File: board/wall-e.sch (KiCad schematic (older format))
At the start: 61 parts, among them J1 Raspberry_Pi_2_3, J10 PCA9685, J11 VL53L0X, J12 VL53L0X, J13 VL53L0X, J14 MotorDrv2, J15 Motor2, J16 IMU, J17 INA219, J18 INA219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

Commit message: Move power monitors onto logic power.
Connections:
- net +5V: now also J17.1 (Pin_1), J18.1 (Pin_1)
- net +5VP: no longer J17.1 (Pin_1), J18.1 (Pin_1)
- net GND: now also J17.2 (Pin_2), J18.2 (Pin_2)
- net GNDA: no longer J17.2 (Pin_2), J18.2 (Pin_2)
- net I2C_ISO_SCL: no longer J17.3 (Pin_3), J18.3 (Pin_3)
- net I2C_ISO_SDA: no longer J17.4 (Pin_4), J18.4 (Pin_4)
- net I2C_M6_SCLK: now also J17.3 (Pin_3), J18.3 (Pin_3)
- net I2C_M6_SDA: now also J17.4 (Pin_4), J18.4 (Pin_4)
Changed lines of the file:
@@
 $EndComp
-$Comp
-L +5VP #PWR045
-U 1 1 5B72CC48
-P 7600 5850
-F 0 "#PWR045" H 7600 5700 50  0001 C CNN
-F 1 "+5VP" H 7600 5990 50  0000 C CNN
-F 2 "" H 7600 5850 50  0001 C CNN
-F 3 "" H 7600 5850 50  0001 C CNN
-	1    7600 5850
-	1    0    0    -1
-$EndComp
-$Comp
-L GNDA #PWR046
-U 1 1 5B72CCD2
-P 7550 6000
-F 0 "#PWR046" H 7550 5750 50  0001 C CNN
-F 1 "GNDA" H 7550 5850 50  0000 C CNN
-F 2 "" H 7550 6000 50  0001 C CNN
-F 3 "" H 7550 6000 50  0001 C CNN
-	1    7550 6000
-	0    1    1    0
-$EndComp
-Text GLabel 7650 6250 0    60   BiDi ~ 0
-I2C_ISO_SDA
-Text GLabel 7650 6150 0    60   Input ~ 0
-I2C_ISO_SCL
 $Comp
 L Conn_01x04 J18
@@
 Text Notes 9300 6300 0    60   ~ 0
 Vcc\nGND\nSCL\nSDA
-$Comp
-L +5VP #PWR047
-U 1 1 5B72DD15
-P 8900 5850
-F 0 "#PWR047" H 8900 5700 50  0001 C CNN
-F 1 "+5VP" H 8900 5990 50  0000 C CNN
-F 2 "" H 8900 5850 50  0001 C CNN
-F 3 "" H 8900 5850 50  0001 C CNN
-	1    8900 5850
-	1    0    0    -1
-$EndComp
-$Comp
-L GNDA #PWR048
-U 1 1 5B72DD1B
-P 8850 6000
-F 0 "#PWR048" H 8850 5750 50  0001 C CNN
-F 1 "GNDA" H 8850 5850 50  0000 C CNN
-F 2 "" H 8850 6000 50  0001 C CNN
-F 3 "" H 8850 6000 50  0001 C CNN
-	1    8850 6000
-	0    1    1    0
-$EndComp
-Text GLabel 8950 6250 0    60   BiDi ~ 0
-I2C_ISO_SDA
-Text GLabel 8950 6150 0    60   Input ~ 0
-I2C_ISO_SCL
 Text Notes 7750 5750 0    60   ~ 0
 Battery sensors\nDifferent addresses!
@@
 Wire Wire Line
 	2700 4500 2700 4600
+Text GLabel 7650 6150 0    60   Input ~ 0
+I2C_M6_SCLK
+Text GLabel 7650 6250 0    60   BiDi ~ 0
+I2C_M6_SDA
+Text GLabel 8950 6250 0    60   BiDi ~ 0
+I2C_M6_SDA
+Text GLabel 8950 6150 0    60   Input ~ 0
+I2C_M6_SCLK
+$Comp
+L +5V #PWR?
+U 1 1 5C045AF6
+P 7600 5850
+F 0 "#PWR?" H 7600 5700 50  0001 C CNN
+F 1 "+5V" H 7600 5990 50  0000 C CNN
+F 2 "" H 7600 5850 50  0001 C CNN
+F 3 "" H 7600 5850 50  0001 C CNN
+	1    7600 5850
+	1    0    0    -1
+$EndComp
+$Comp
+L +5V #PWR?
+U 1 1 5C045B84
+P 8900 5850
+F 0 "#PWR?" H 8900 5700 50  0001 C CNN
+F 1 "+5V" H 8900 5990 50  0000 C CNN
+F 2 "" H 8900 5850 50  0001 C CNN
+F 3 "" H 8900 5850 50  0001 C CNN
+	1    8900 5850
+	1    0    0    -1
+$EndComp
+$Comp
+L GND #PWR?
+U 1 1 5C045C8E
+P 7550 6000
+F 0 "#PWR?" H 7550 5750 50  0001 C CNN
+F 1 "GND" H 7550 5850 50  0000 C CNN
+F 2 "" H 7550 6000 50  0001 C CNN
+F 3 "" H 7550 6000 50  0001 C CNN
+	1    7550 6000
+	0    1    1    0
+$EndComp
+$Comp
+L GND #PWR?
+U 1 1 5C045D94
+P 8850 6000
+F 0 "#PWR?" H 8850 5750 50  0001 C CNN
+F 1 "GND" H 8850 5850 50  0000 C CNN
+F 2 "" H 8850 6000 50  0001 C CNN
+F 3 "" H 8850 6000 50  0001 C CNN
+	1    8850 6000
+	0    1    1    0
+$EndComp
 $EndSCHEMATC

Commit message: Tweaks.
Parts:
- added C15: 470u, Capacitors_THT:CP_Radial_D8.0mm_P3.50mm, symbol CP
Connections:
- net +5V: now also C15.1
- net GND: now also C15.2
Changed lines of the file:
@@
 Connection ~ 9850 2950
 $Comp
-L GND #PWR049
+L GND #PWR045
 U 1 1 5BF31737
 P 6050 7500
-F 0 "#PWR049" H 6050 7250 50  0001 C CNN
+F 0 "#PWR045" H 6050 7250 50  0001 C CNN
 F 1 "GND" H 6050 7350 50  0000 C CNN
 F 2 "" H 6050 7500 50  0001 C CNN
@@
 $EndComp
 $Comp
-L GNDA #PWR050
+L GNDA #PWR046
 U 1 1 5BF317C1
 P 6450 7500
-F 0 "#PWR050" H 6450 7250 50  0001 C CNN
+F 0 "#PWR046" H 6450 7250 50  0001 C CNN
 F 1 "GNDA" H 6450 7350 50  0000 C CNN
 F 2 "" H 6450 7500 50  0001 C CNN
@@
 	9750 2850 9800 2850
 $Comp
-L PWR_FLAG #FLG051
+L PWR_FLAG #FLG047
 U 1 1 5C026CFB
 P 7750 3450
-F 0 "#FLG051" H 7750 3525 50  0001 C CNN
+F 0 "#FLG047" H 7750 3525 50  0001 C CNN
 F 1 "PWR_FLAG" H 7750 3600 50  0000 C CNN
 F 2 "" H 7750 3450 50  0001 C CNN
@@
 Connection ~ 7650 3700
 $Comp
-L PWR_FLAG #FLG052
+L PWR_FLAG #FLG048
 U 1 1 5C027A7F
 P 7950 3800
-F 0 "#FLG052" H 7950 3875 50  0001 C CNN
+F 0 "#FLG048" H 7950 3875 50  0001 C CNN
 F 1 "PWR_FLAG" H 7950 3950 50  0000 C CNN
 F 2 "" H 7950 3800 50  0001 C CNN
@@
 $EndComp
 $Comp
-L PWR_FLAG #FLG053
+L PWR_FLAG #FLG049
 U 1 1 5C027C73
 P 4250 3600
-F 0 "#FLG053" H 4250 3675 50  0001 C CNN
+F 0 "#FLG049" H 4250 3675 50  0001 C CNN
 F 1 "PWR_FLAG" H 4250 3750 50  0000 C CNN
 F 2 "" H 4250 3600 50  0001 C CNN
@@
 $EndComp
 $Comp
-L PWR_FLAG #FLG054
+L PWR_FLAG #FLG050
 U 1 1 5C027CFF
 P 4250 3300
-F 0 "#FLG054" H 4250 3375 50  0001 C CNN
+F 0 "#FLG050" H 4250 3375 50  0001 C CNN
 F 1 "PWR_FLAG" H 4250 3450 50  0000 C CNN
 F 2 "" H 4250 3300 50  0001 C CNN
@@
 NoConn ~ 6900 2800
 $Comp
-L +3.3V #PWR055
+L +3.3V #PWR051
 U 1 1 5C02CA19
 P 2200 700
-F 0 "#PWR055" H 2200 550 50  0001 C CNN
+F 0 "#PWR051" H 2200 550 50  0001 C CNN
 F 1 "+3.3V" H 2200 840 50  0000 C CNN
 F 2 "" H 2200 700 50  0001 C CNN
@@
 	1250 1650 1100 1650
 $Comp
-L +3.3V #PWR056
+L +3.3V #PWR052
 U 1 1 5C027A8A
 P 4750 6350
-F 0 "#PWR056" H 4750 6200 50  0001 C CNN
+F 0 "#PWR052" H 4750 6200 50  0001 C CNN
 F 1 "+3.3V" H 4750 6490 50  0000 C CNN
 F 2 "" H 4750 6350 50  0001 C CNN
@@
 $EndComp
 $Comp
-L +5V #PWR057
+L +5V #PWR053
 U 1 1 5C0303D2
 P 2700 4100
-F 0 "#PWR057" H 2700 3950 50  0001 C CNN
+F 0 "#PWR053" H 2700 3950 50  0001 C CNN
 F 1 "+5V" H 2700 4240 50  0000 C CNN
 F 2 "" H 2700 4100 50  0001 C CNN
@@
 $EndComp
 $Comp
-L GND #PWR058
+L GND #PWR054
 U 1 1 5C030460
 P 2700 4600
-F 0 "#PWR058" H 2700 4350 50  0001 C CNN
+F 0 "#PWR054" H 2700 4350 50  0001 C CNN
 F 1 "GND" H 2700 4450 50  0000 C CNN
 F 2 "" H 2700 4600 50  0001 C CNN
@@
 I2C_M6_SCLK
 $Comp
-L +5V #PWR?
+L +5V #PWR055
 U 1 1 5C045AF6
 P 7600 5850
-F 0 "#PWR?" H 7600 5700 50  0001 C CNN
+F 0 "#PWR055" H 7600 5700 50  0001 C CNN
 F 1 "+5V" H 7600 5990 50  0000 C CNN
 F 2 "" H 7600 5850 50  0001 C CNN
@@
 $EndComp
 $Comp
-L +5V #PWR?
+L +5V #PWR056
 U 1 1 5C045B84
 P 8900 5850
-F 0 "#PWR?" H 8900 5700 50  0001 C CNN
+F 0 "#PWR056" H 8900 5700 50  0001 C CNN
 F 1 "+5V" H 8900 5990 50  0000 C CNN
 F 2 "" H 8900 5850 50  0001 C CNN
@@
 $EndComp
 $Comp
-L GND #PWR?
+L GND #PWR057
 U 1 1 5C045C8E
 P 7550 6000
-F 0 "#PWR?" H 7550 5750 50  0001 C CNN
+F 0 "#PWR057" H 7550 5750 50  0001 C CNN
 F 1 "GND" H 7550 5850 50  0000 C CNN
 F 2 "" H 7550 6000 50  0001 C CNN
@@
 $EndComp
 $Comp
-L GND #PWR?
+L GND #PWR058
 U 1 1 5C045D94
 P 8850 6000
-F 0 "#PWR?" H 8850 5750 50  0001 C CNN
+F 0 "#PWR058" H 8850 5750 50  0001 C CNN
 F 1 "GND" H 8850 5850 50  0000 C CNN
 F 2 "" H 8850 6000 50  0001 C CNN
@@
 	0    1    1    0
 $EndComp
+$Comp
+L CP C15
+U 1 1 5C0583D5
+P 3550 3450
+F 0 "C15" H 3575 3550 50  0000 L CNN
+F 1 "470u" H 3575 3350 50  0000 L CNN
+F 2 "Capacitors_THT:CP_Radial_D8.0mm_P3.50mm" H 3588 3300 50  0001 C CNN
+F 3 "" H 3550 3450 50  0001 C CNN
+	1    3550 3450
+	1    0    0    -1
+$EndComp
+$Comp
+L +5V #PWR059
+U 1 1 5C0584F8
+P 3550 3200
+F 0 "#PWR059" H 3550 3050 50  0001 C CNN
+F 1 "+5V" H 3550 3340 50  0000 C CNN
+F 2 "" H 3550 3200 50  0001 C CNN
+F 3 "" H 3550 3200 50  0001 C CNN
+	1    3550 3200
+	1    0    0    -1
+$EndComp
+Wire Wire Line
+	3550 3200 3550 3300
+$Comp
+L GND #PWR060
+U 1 1 5C05878D
+P 3550 3700
+F 0 "#PWR060" H 3550 3450 50  0001 C CNN
+F 1 "GND" H 3550 3550 50  0000 C CNN
+F 2 "" H 3550 3700 50  0001 C CNN
+F 3 "" H 3550 3700 50  0001 C CNN
+	1    3550 3700
+	1    0    0    -1
+$EndComp
+Wire Wire Line
+	3550 3700 3550 3600
 $EndSCHEMATC

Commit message: Add bridge between 5V rails.
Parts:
- added J20: GS2, Connectors:GS2, symbol GS2
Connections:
- net +5V: now also J20.1 (G1)
- net +5VP: now also J20.2 (G2)
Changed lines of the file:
@@
 Wire Wire Line
 	3550 3700 3550 3600
+$Comp
+L GS2 J20
+U 1 1 5C06784D
+P 5750 7450
+F 0 "J20" H 5850 7600 50  0000 C CNN
+F 1 "GS2" H 5850 7301 50  0000 C CNN
+F 2 "Connectors:GS2" V 5824 7450 50  0001 C CNN
+F 3 "" H 5750 7450 50  0001 C CNN
+	1    5750 7450
+	0    1    1    0
+$EndComp
+$Comp
+L +5V #PWR061
+U 1 1 5C06790B
+P 5900 7250
+F 0 "#PWR061" H 5900 7100 50  0001 C CNN
+F 1 "+5V" H 5900 7390 50  0000 C CNN
+F 2 "" H 5900 7250 50  0001 C CNN
+F 3 "" H 5900 7250 50  0001 C CNN
+	1    5900 7250
+	1    0    0    -1
+$EndComp
+Wire Wire Line
+	5950 7450 5950 7250
+Wire Wire Line
+	5950 7250 5900 7250
+Wire Wire Line
+	5600 7250 5550 7250
+Wire Wire Line
+	5550 7250 5550 7450
+$Comp
+L +5VP #PWR?
+U 1 1 5C068358
+P 5600 7250
+F 0 "#PWR?" H 5600 7100 50  0001 C CNN
+F 1 "+5VP" H 5600 7390 50  0000 C CNN
+F 2 "" H 5600 7250 50  0001 C CNN
+F 3 "" H 5600 7250 50  0001 C CNN
+	1    5600 7250
+	1    0    0    -1
+$EndComp
 $EndSCHEMATC

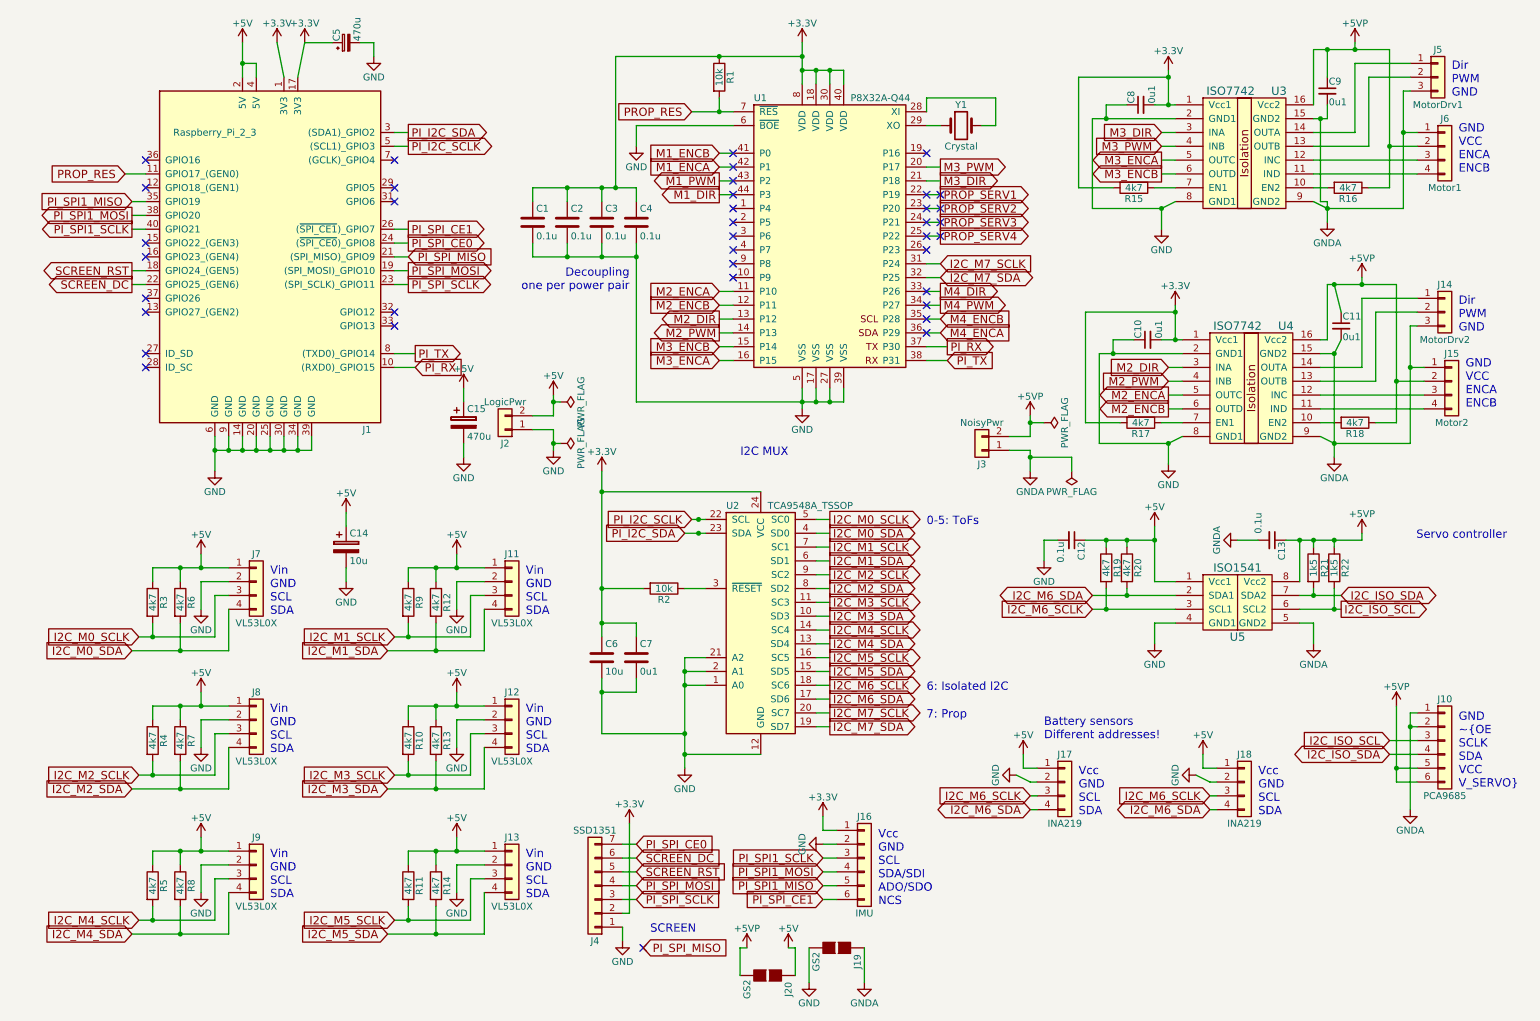
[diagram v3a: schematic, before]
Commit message: Connect IMU to SPI0, add pour to mux ground.
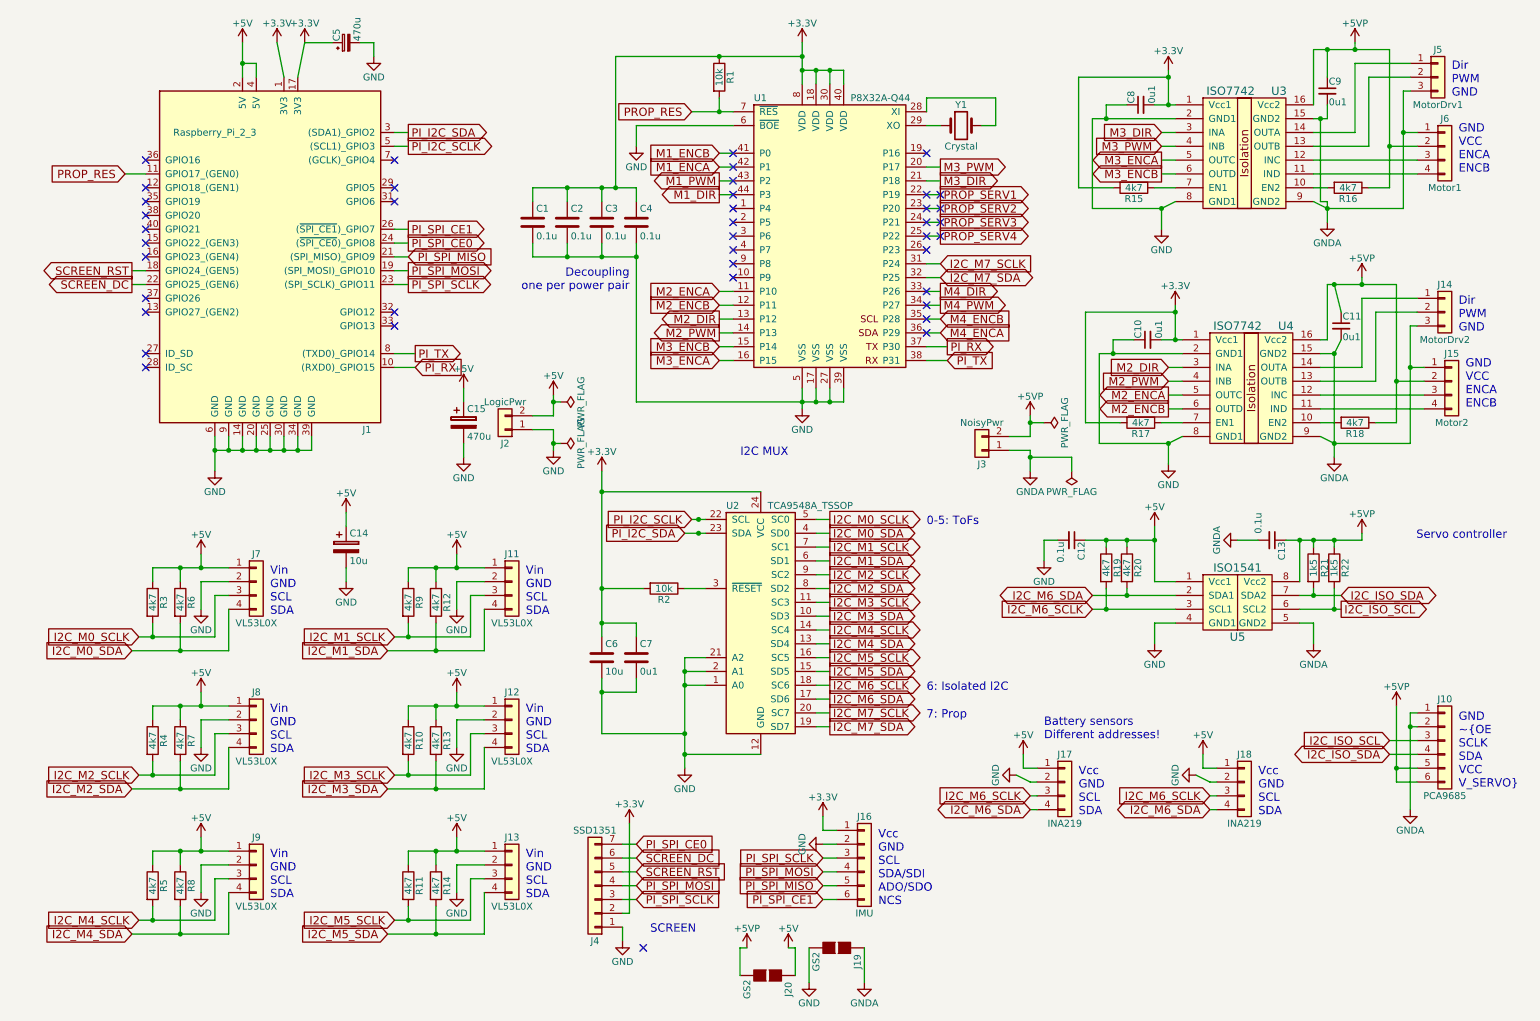
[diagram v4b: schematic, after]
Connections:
- net PI_SPI_MISO: now also J16.5 (Pin_5)
- net PI_SPI_MOSI: now also J16.4 (Pin_4)
- net PI_SPI_SCLK: now also J16.3 (Pin_3)
- net PI_SPI1_MISO: no longer names the net of J1.35 (GPIO19)
- net PI_SPI1_MISO: no longer J16.5 (Pin_5)
- net PI_SPI1_MOSI: no longer names the net of J1.38 (GPIO20)
- net PI_SPI1_MOSI: no longer J16.4 (Pin_4)
- net PI_SPI1_SCLK: no longer names the net of J1.40 (GPIO21)
- net PI_SPI1_SCLK: no longer J16.3 (Pin_3)
- no-connect marks 38 -> 41
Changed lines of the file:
@@
 $EndComp
 Text GLabel 6150 6600 0    60   Input ~ 0
-PI_SPI1_SCLK
+PI_SPI_SCLK
 Text GLabel 6150 6700 0    60   Input ~ 0
-PI_SPI1_MOSI
+PI_SPI_MOSI
 Text GLabel 6150 6900 0    60   Input ~ 0
 PI_SPI_CE1
 Text GLabel 6150 6800 0    60   Input ~ 0
-PI_SPI1_MISO
-Text GLabel 1150 1850 0    60   Input ~ 0
-PI_SPI1_MISO
-Text GLabel 1150 1950 0    60   Output ~ 0
-PI_SPI1_MOSI
-Text GLabel 1150 2050 0    60   Output ~ 0
-PI_SPI1_SCLK
+PI_SPI_MISO
 $Comp
 L GNDA #PWR043
@@
 Wire Wire Line
 	7000 2300 6900 2300
-Wire Wire Line
-	1150 1850 1250 1850
-Wire Wire Line
-	1150 1950 1250 1950
-Wire Wire Line
-	1150 2050 1250 2050
 Wire Wire Line
 	6150 6700 6250 6700
@@
 NoConn ~ 1250 1750
 NoConn ~ 1250 1550
-Text GLabel 4850 7250 2    60   Input ~ 0
-PI_SPI_MISO
 NoConn ~ 4850 7250
 NoConn ~ 6900 2200
@@
 	1    0    0    -1
 $EndComp
+NoConn ~ 1250 2050
+NoConn ~ 1250 1950
+NoConn ~ 1250 1850
 $EndSCHEMATC
